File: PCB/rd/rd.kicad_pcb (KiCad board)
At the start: 2 copper layers, 18.5 x 32 mm, 13 parts, among them U1 GL823K-HCY04

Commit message: wow
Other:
- board text added: "#dongle"
- board text added: "@jblitzar"

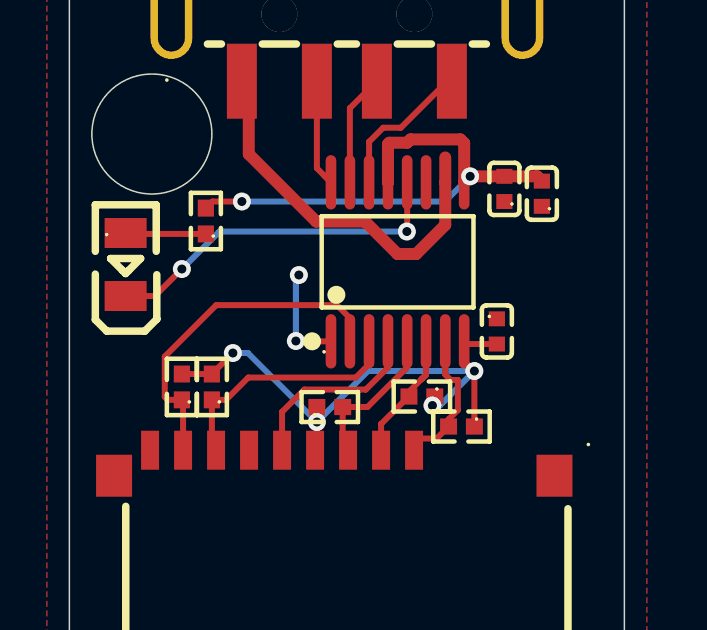
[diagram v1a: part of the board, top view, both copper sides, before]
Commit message: emergency 47uF addition
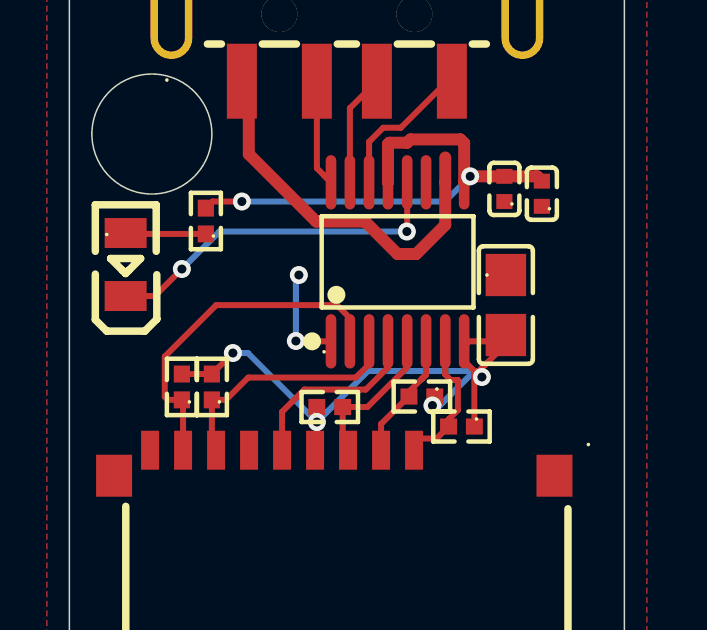
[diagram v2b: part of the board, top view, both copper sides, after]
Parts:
- removed C2: 100nF, easyeda2kicad:C0402
- added C4: 47uF, easyeda2kicad:C0805, F.Cu at (85.3, 86.7)
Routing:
- net /PMOS: track 19.0 -> 22.2 mm
